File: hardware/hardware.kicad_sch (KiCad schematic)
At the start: 162 parts, among them J1 USB_B_Micro, J2 RJ45_Hanrun_HR911105A_Horizon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, J3 Conn_02x05_Odd_Even, J4 Conn_02x03_Odd_Even, J5 Conn_01x02, U10 CH32V003F4P6, U11 CH32V003F4P6, U12 CH32V003F4P6, U13 CH32V003F4P6, U14 CH32V003F4P6, U15 CH32V003F4P6, U16 CH32V003F4P6, U17 CH32V003F4P6, U18 CH32V003F4P6, U19 CH32V003F4P6, U2 CH32V003F4P6, U20 CH32V003F4P6, U21 CH32V003F4P6, U22 CH32V003F4P6, U23 CH32V003F4P6, U24 CH32V003F4P6, U25 CH32V003F4P6, U26 CH32V003F4P6, U27 CH32V003F4P6, U28 CH32V307RCT6, U3 AMS1117-3.3, U4 CH340C, U5 CH32V003F4P6, U6 CH32V003F4P6, U7 CH32V003F4P6, U8 CH32V003F4P6, U9 CH32V003F4P6

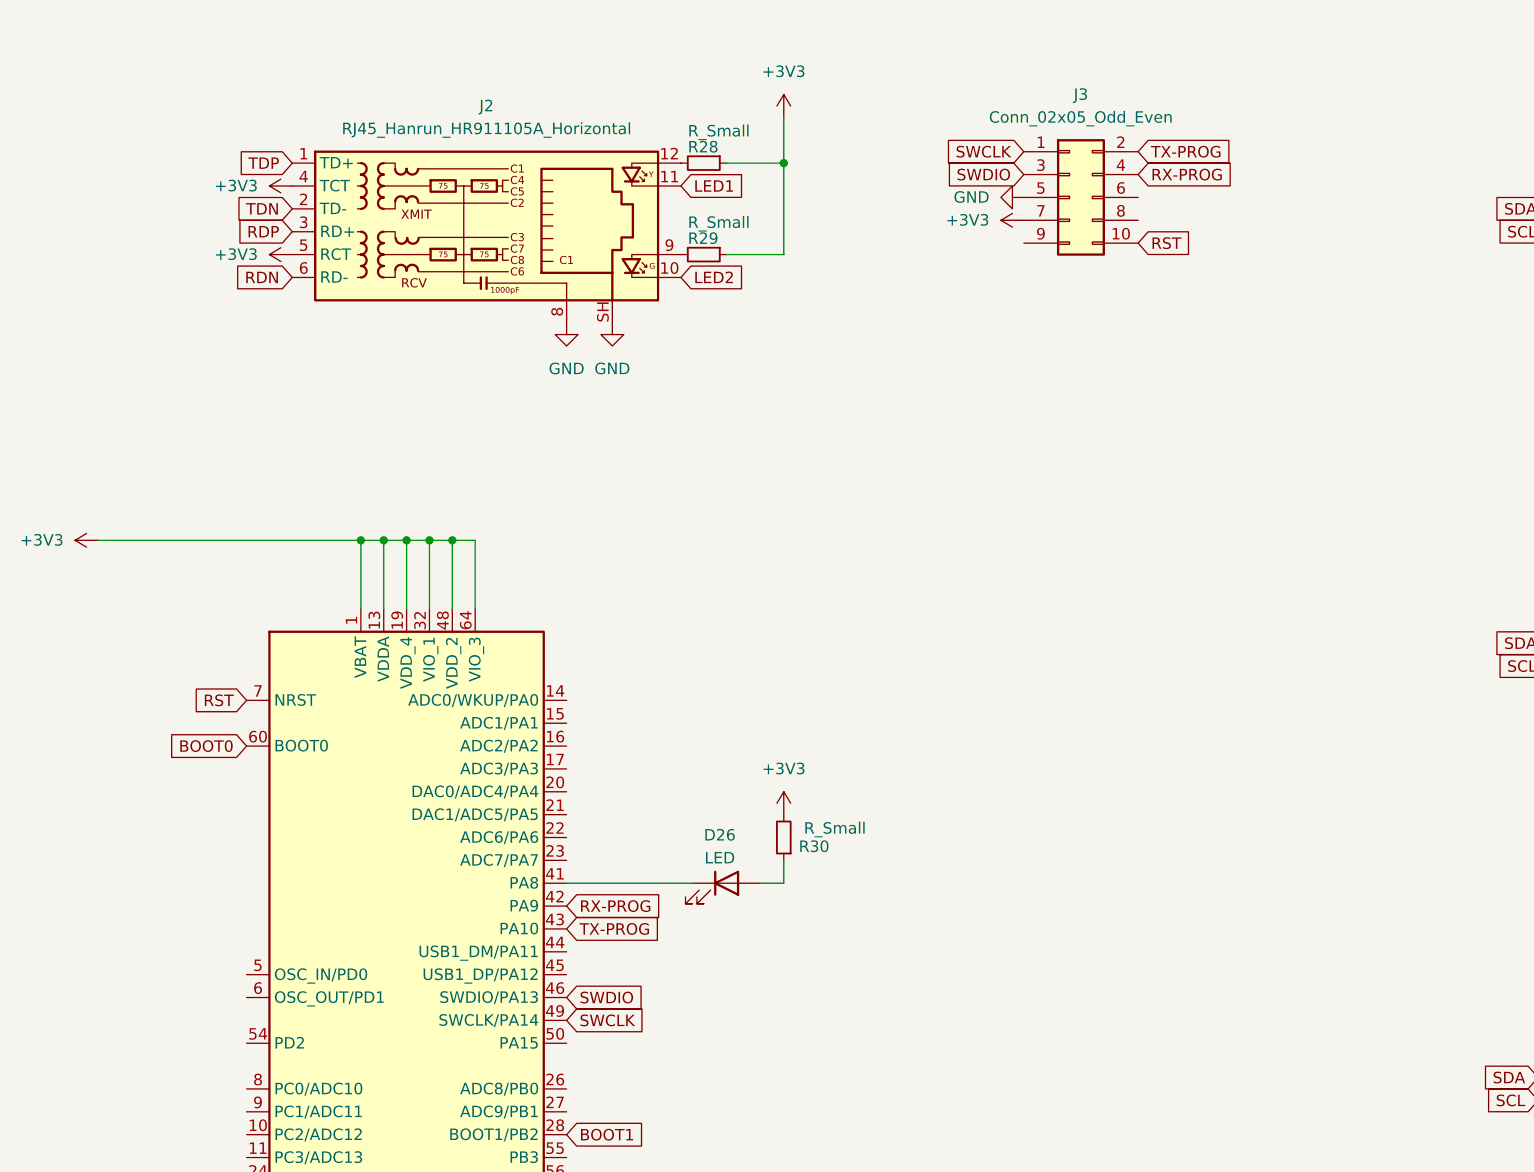
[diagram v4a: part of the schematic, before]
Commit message: add external crystal
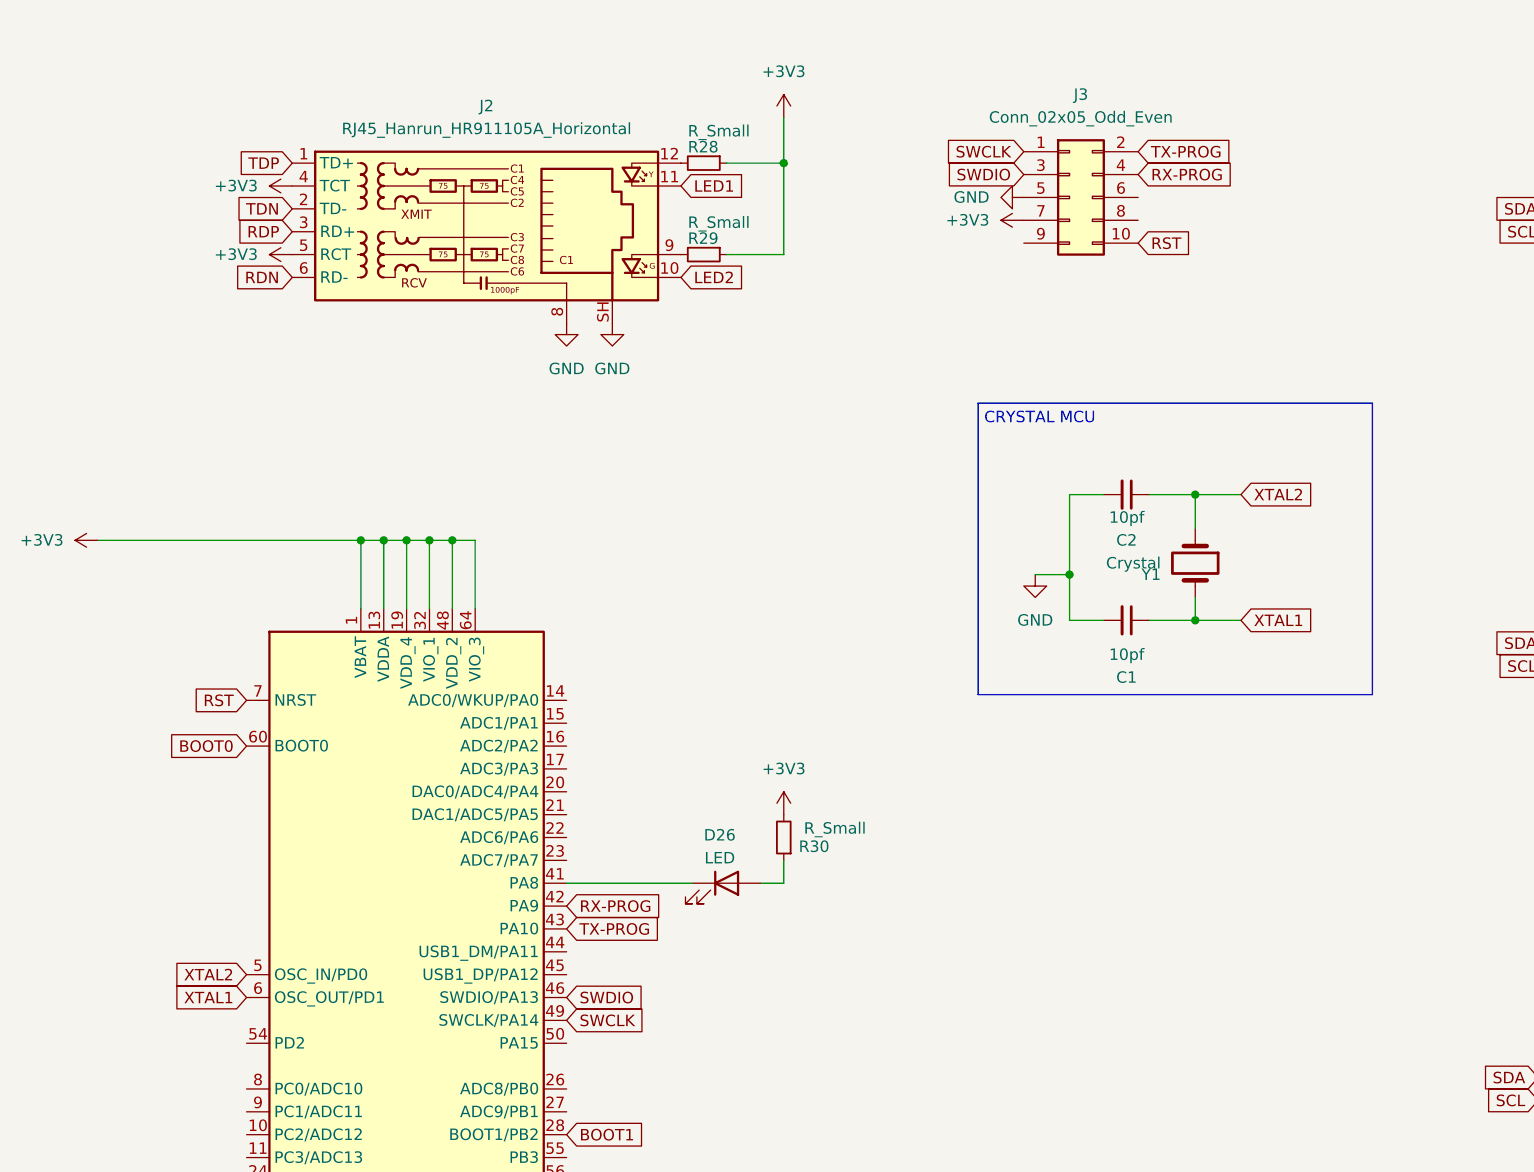
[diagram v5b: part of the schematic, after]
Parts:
- added C1, C2: 10pf, Capacitor_SMD:C_0603_1608Metric, symbol Device:C_Small
- added Y1: Crystal, Crystal:Crystal_SMD_3225-4Pin_3.2x2.5mm, symbol Device:Crystal
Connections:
- net GND: now also C1.2, C2.2
- net XTAL2: now reaches U28.5 (OSC_IN/PD0)
- net XTAL2: now also C2.1, Y1.1
- net XTAL1: now reaches U28.6 (OSC_OUT/PD1)
- net XTAL1: now also C1.1, Y1.2
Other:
- note added: "CRYSTAL MCU"

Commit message: update crystal + slave reset pull up
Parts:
- removed Y1: Crystal, Crystal:Crystal_SMD_3225-4Pin_3.2x2.5mm, symbol Device:Crystal
- added R1, R2, R27, R33, R34, R35, R36, R37, R38, R39, R40, R41, R42, R43, R44, R45, R46, R47, R48, R49, R50, R51, R52, R53: R_Small, Resistor_SMD:R_0603_1608Metric, symbol Device:R_Small
- added TP25, TP26, TP27, TP28, TP29, TP30, TP31, TP32, TP33, TP34, TP35, TP36, TP37, TP38, TP39, TP40, TP41, TP42, TP43, TP44, TP45, TP46, TP47, TP48: TestPoint, TestPoint:TestPoint_Pad_1.0x1.0mm, symbol Connector:TestPoint
- added Y1: Crystal_GND24, symbol Device:Crystal_GND24
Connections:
- net +3V3: now also R1.2, R2.2, R27.2, R33.2, R34.2, R35.2, R36.2, R37.2, R38.2, R39.2, R40.2, R41.2, R42.2, R43.2, R44.2, R45.2, R46.2, R47.2, R48.2, R49.2, R50.2, R51.2, R52.2, R53.2
- net GND: now also Y1.2, Y1.4
- net XTAL1: now also Y1.1
- net XTAL2: now also Y1.3
- net at U26.4 (PD7/~{RST}/T2CH4/OPP1): now also R51.1, TP46.1
- net at U10.4 (PD7/~{RST}/T2CH4/OPP1): now also R27.1, TP27.1
- net at U12.4 (PD7/~{RST}/T2CH4/OPP1): now also R43.1, TP38.1
- net at U27.4 (PD7/~{RST}/T2CH4/OPP1): now also R50.1, TP45.1
- net at U18.4 (PD7/~{RST}/T2CH4/OPP1): now also R41.1, TP36.1
- net at U17.4 (PD7/~{RST}/T2CH4/OPP1): now also R40.1, TP35.1
- net at U15.4 (PD7/~{RST}/T2CH4/OPP1): now also R46.1, TP41.1
- net at U9.4 (PD7/~{RST}/T2CH4/OPP1): now also R33.1, TP28.1
- net at U21.4 (PD7/~{RST}/T2CH4/OPP1): now also R48.1, TP43.1
- net at U19.4 (PD7/~{RST}/T2CH4/OPP1): now also R42.1, TP37.1
- net at U13.4 (PD7/~{RST}/T2CH4/OPP1): now also R44.1, TP39.1
- net at U11.4 (PD7/~{RST}/T2CH4/OPP1): now also R2.1, TP26.1
- net at U23.4 (PD7/~{RST}/T2CH4/OPP1): now also R1.1, TP25.1
- net at U2.4 (PD7/~{RST}/T2CH4/OPP1): now also R38.1, TP33.1
- net at U6.4 (PD7/~{RST}/T2CH4/OPP1): now also R36.1, TP31.1
- net at U7.4 (PD7/~{RST}/T2CH4/OPP1): now also R35.1, TP30.1
- net at U14.4 (PD7/~{RST}/T2CH4/OPP1): now also R45.1, TP40.1
- net at U25.4 (PD7/~{RST}/T2CH4/OPP1): now also R52.1, TP47.1
- net at U22.4 (PD7/~{RST}/T2CH4/OPP1): now also R47.1, TP42.1
- net at U16.4 (PD7/~{RST}/T2CH4/OPP1): now also R39.1, TP34.1
- net at U20.4 (PD7/~{RST}/T2CH4/OPP1): now also R49.1, TP44.1
- net at U24.4 (PD7/~{RST}/T2CH4/OPP1): now also R53.1, TP48.1
- net at U5.4 (PD7/~{RST}/T2CH4/OPP1): now also R37.1, TP32.1
- net at U8.4 (PD7/~{RST}/T2CH4/OPP1): now also R34.1, TP29.1

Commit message: crystal to gnd
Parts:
- Y1: footprint (none) -> Crystal:Crystal_SMD_3225-4Pin_3.2x2.5mm_HandSoldering
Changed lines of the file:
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@@
 			)
 		)
-		(property "Footprint" ""
+		(property "Footprint" "Crystal:Crystal_SMD_3225-4Pin_3.2x2.5mm_HandSoldering"
 			(at 156.21 176.53 0)
 			(effects

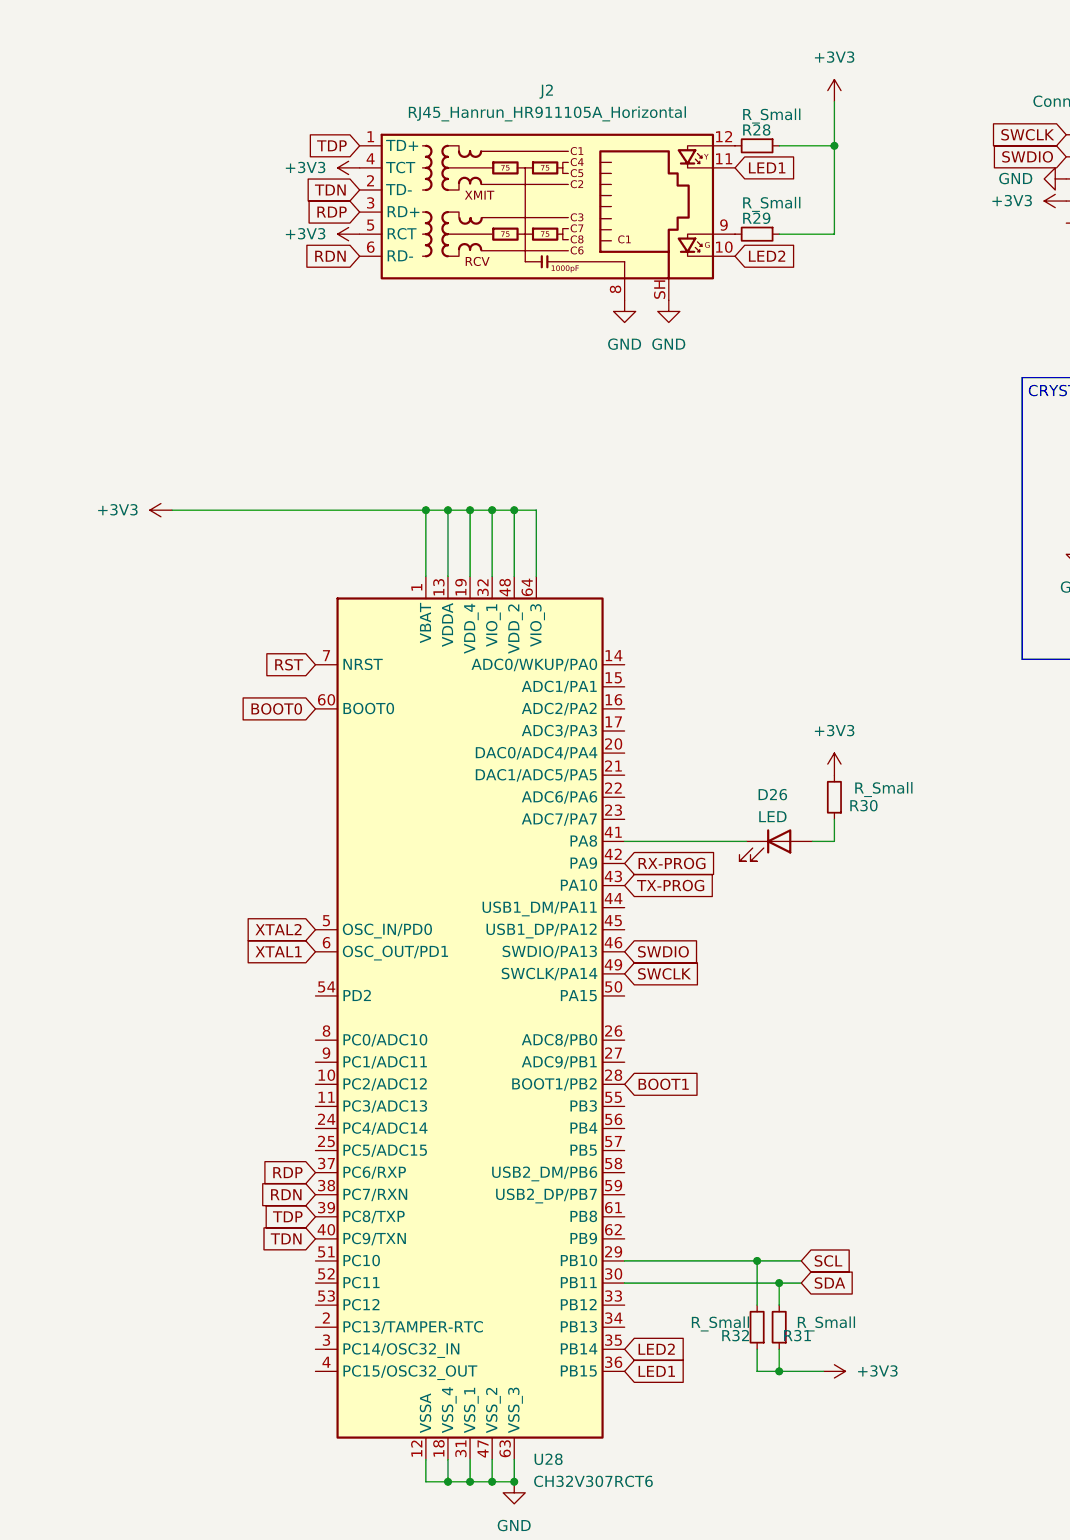
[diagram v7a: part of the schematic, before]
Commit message: update ehernet wiring
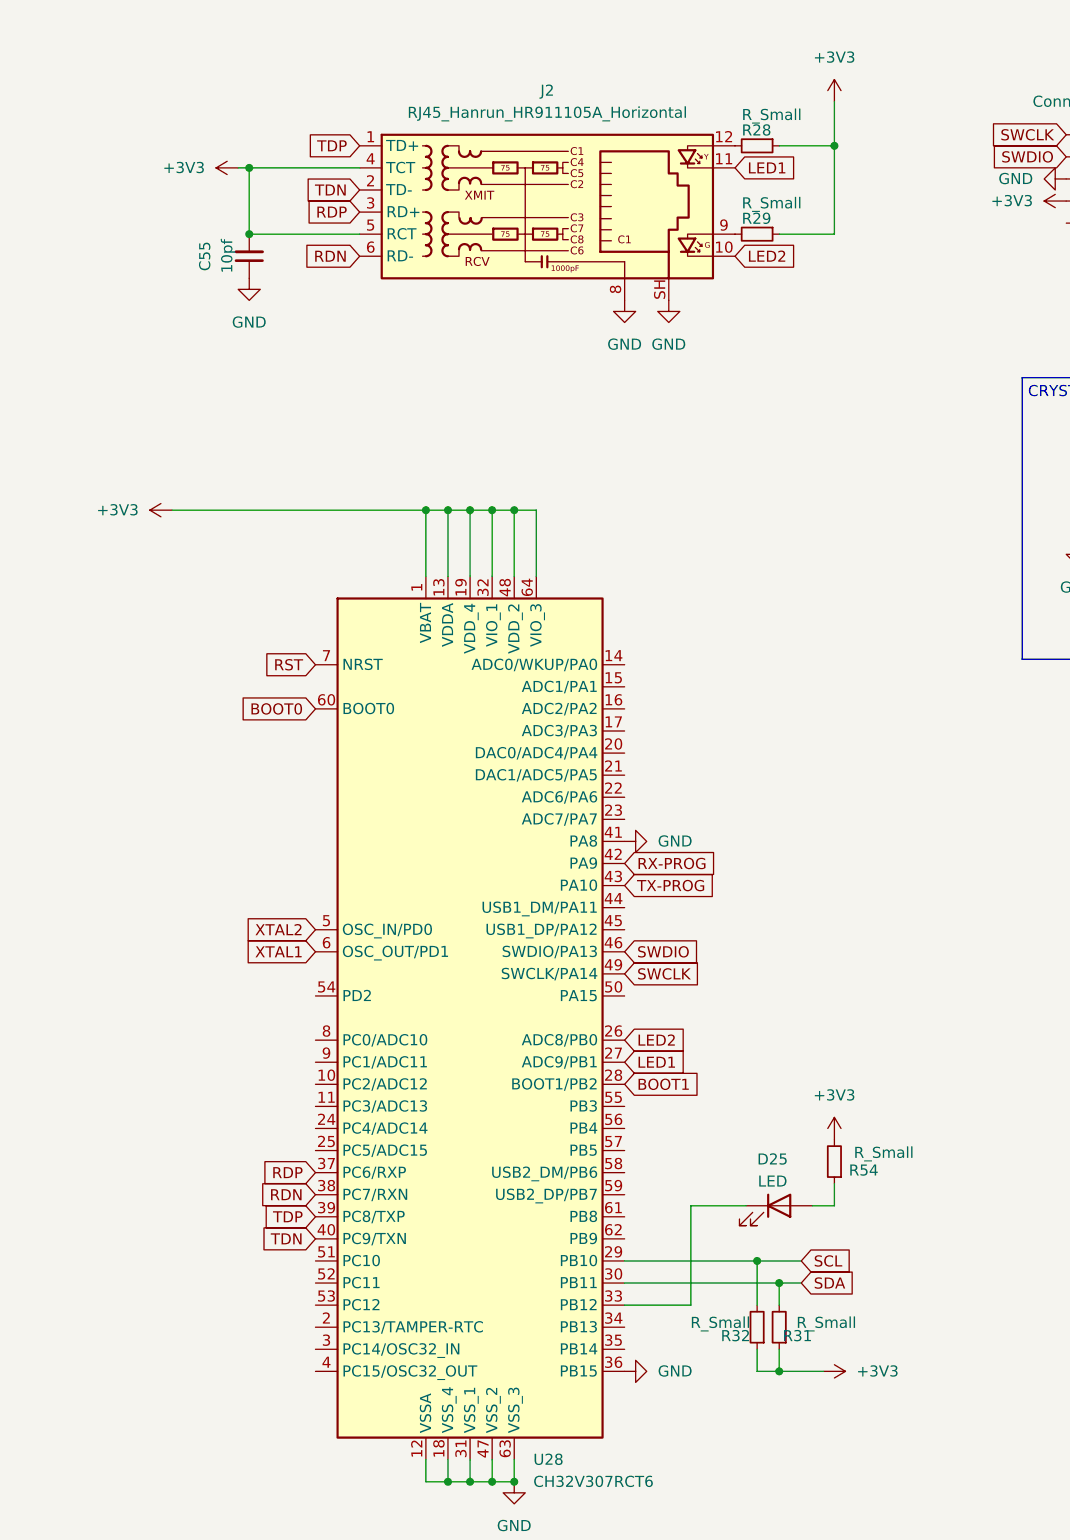
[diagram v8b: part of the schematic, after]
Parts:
- removed D26: LED, LED_SMD:LED_0603_1608Metric, symbol Device:LED
- removed R30: R_Small, Resistor_SMD:R_0603_1608Metric, symbol Device:R_Small
- added C55: 10pf, Capacitor_SMD:C_0603_1608Metric, symbol Device:C_Small
- added D25: LED, LED_SMD:LED_0603_1608Metric, symbol Device:LED
- added R54: R_Small, Resistor_SMD:R_0603_1608Metric, symbol Device:R_Small
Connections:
- net +3V3: now also C55.2, R54.2
- net GND: now also U28.36 (PB15), U28.41 (PA8), C55.1
- net LED1: now also U28.27 (ADC9/PB1); no longer U28.36 (PB15)
- net LED2: now also U28.26 (ADC8/PB0); no longer U28.35 (PB14)
- net at U28.33 (PB12): now also D25.1 (K)
- new net: D25.2 (A), R54.1
